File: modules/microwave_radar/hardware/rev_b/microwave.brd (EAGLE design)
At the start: 68.1 x 66 mm, 56 parts, among them J1 MODULE_GENERIC, J2 TC2030-JLINK-L, U1 SAM4LC8AA, U2 TLV62130, U3 MSGEQ7, U4 HB100, U5 OP284E_SEPARATE

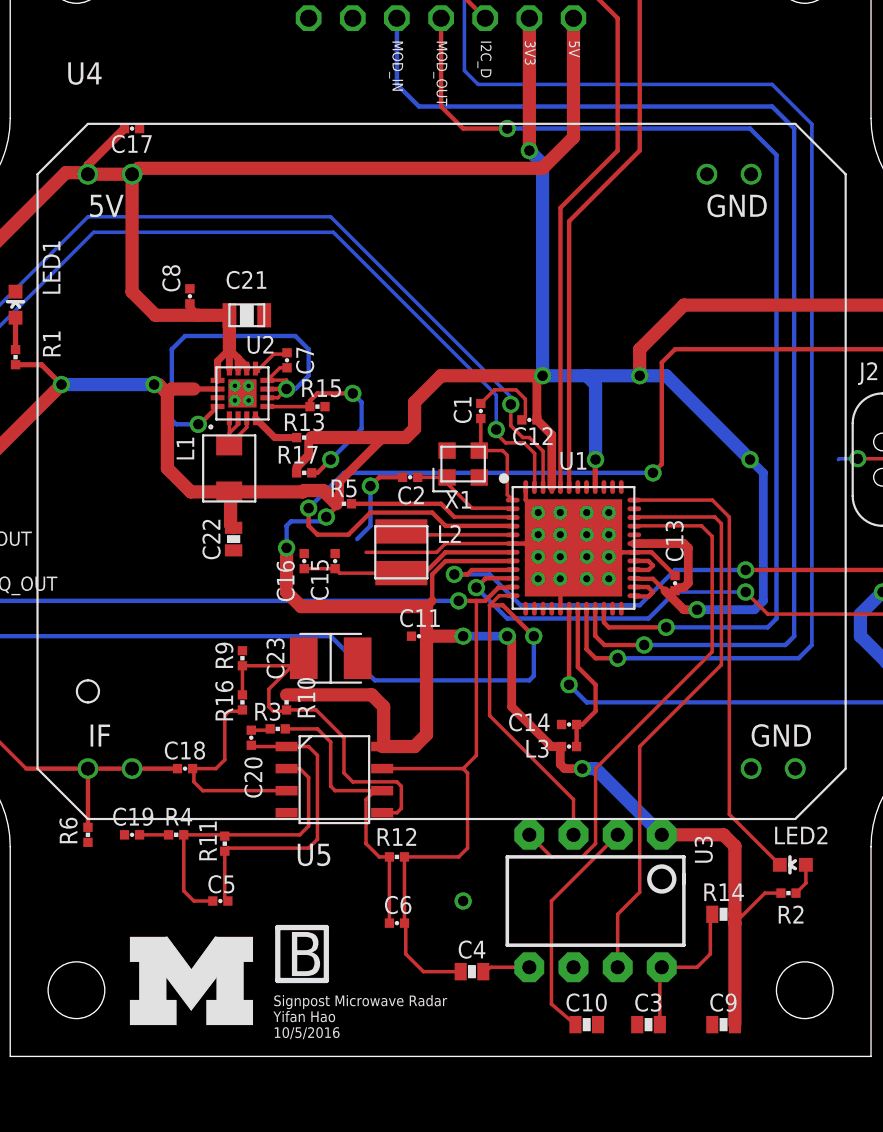
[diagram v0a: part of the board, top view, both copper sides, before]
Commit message: Fix MSGEQ7 swapped pins!!!
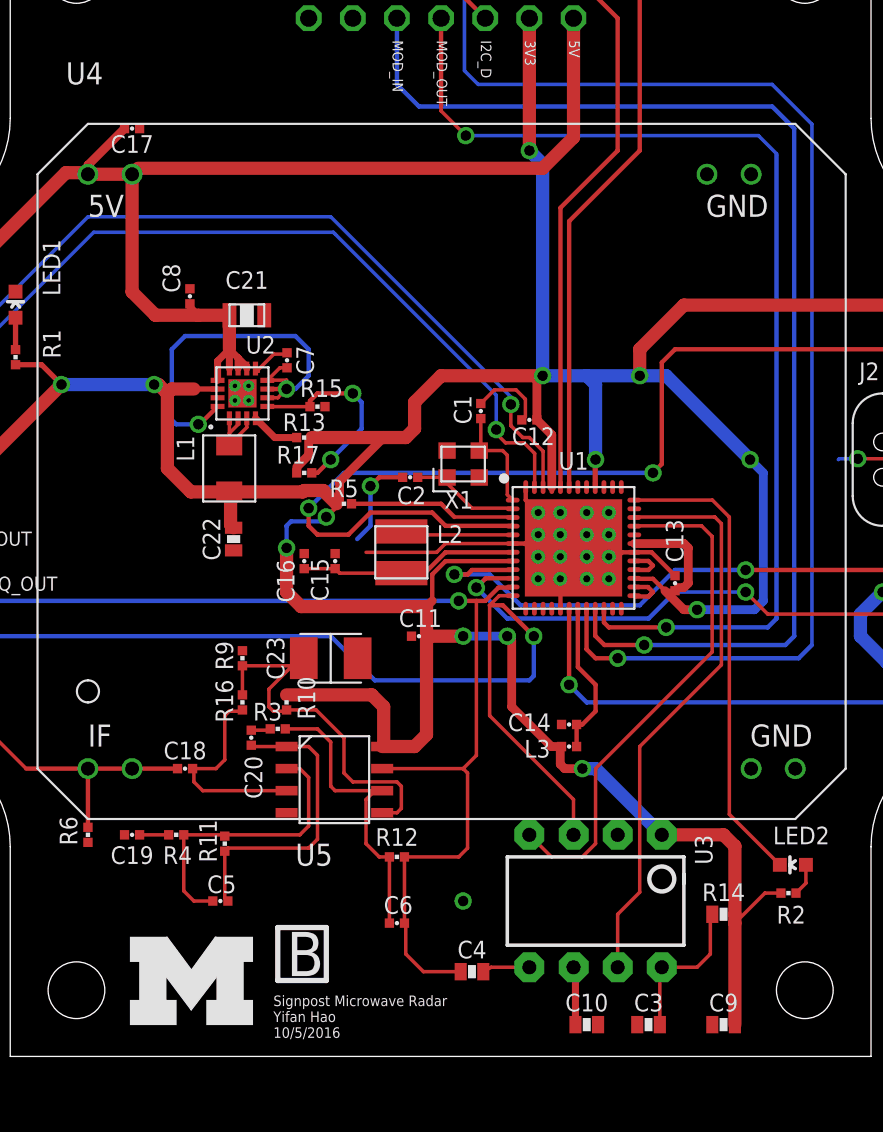
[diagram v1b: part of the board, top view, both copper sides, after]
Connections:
- net GND: now also U3.2; no longer U3.6
- net N$7: now also U3.6; no longer U3.2
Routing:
- net N$7: track 13.1 -> 3.41 mm
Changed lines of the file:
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@@
 </element>
 <element name="R4" library="passives" package="0402_RES" value="10k" x="21.59" y="15.24" smashed="yes" rot="R180">
-<attribute name="NAME" x="21.7424" y="16.7894" size="1.016" layer="25" font="vector" ratio="12" rot="R180" align="bottom-center"/>
+<attribute name="NAME" x="21.6662" y="14.5796" size="1.016" layer="25" font="vector" ratio="12" rot="R180" align="bottom-center"/>
 <attribute name="VALUE" x="21.59" y="16.637" size="1.016" layer="27" font="vector" ratio="12" rot="R180" align="bottom-center"/>
 <attribute name="DIGIKEY" value="1276-3431-1-ND" x="21.59" y="15.24" size="1.778" layer="27" rot="R180" display="off"/>
 </element>
 <element name="C19" library="passives" package="0402_CAP" value="4.7uF" x="19.05" y="15.24" smashed="yes">
-<attribute name="NAME" x="19.1262" y="15.7734" size="1.016" layer="25" font="vector" ratio="12" align="bottom-center"/>
+<attribute name="NAME" x="19.05" y="13.5636" size="1.016" layer="25" font="vector" ratio="12" align="bottom-center"/>
 <attribute name="DIGIKEY" value="1276-1481-1-ND" x="19.05" y="15.24" size="1.778" layer="27" display="off"/>
 </element>
@@
 <contactref element="U2" pad="6"/>
 <contactref element="R15" pad="1"/>
-<contactref element="U3" pad="6"/>
 <wire x1="47.954" y1="31.496" x2="47.95" y2="31.5" width="0.2032" layer="1"/>
 <polygon width="0.2032" layer="1" isolate="0.254">
@@
 <contactref element="C9" pad="1"/>
 <contactref element="C3" pad="2"/>
-<contactref element="C10" pad="2"/>
 <via x="38.1" y="11.43" extent="1-16" drill="0.6"/>
 <wire x1="27.9654" y1="42.11193125" x2="27.55193125" y2="42.11193125" width="0.2032" layer="1"/>
@@
 <wire x1="41.6814" y1="39.32046875" x2="41.47693125" y2="39.116" width="0.2032" layer="1"/>
 <contactref element="LED1" pad="C"/>
+<contactref element="C10" pad="2"/>
+<contactref element="U3" pad="2"/>
 </signal>
 <signal name="CONTROLLER_XIN">
@@
 <wire x1="55.626" y1="27.178" x2="56.134" y2="27.686" width="0.254" layer="16"/>
 <wire x1="56.134" y1="27.686" x2="56.134" y2="54.356" width="0.254" layer="16"/>
-<wire x1="56.134" y1="54.356" x2="54.61" y2="55.88" width="0.254" layer="16"/>
-<wire x1="54.61" y1="55.88" x2="40.64" y2="55.88" width="0.254" layer="16"/>
-<via x="40.64" y="55.88" extent="1-16" drill="0.6"/>
-<wire x1="40.64" y1="55.88" x2="38.1" y2="55.88" width="0.254" layer="1"/>
-<wire x1="38.1" y1="55.88" x2="36.83" y2="57.15" width="0.254" layer="1"/>
 <wire x1="36.83" y1="57.15" x2="36.83" y2="62.23" width="0.254" layer="1"/>
+<wire x1="56.134" y1="54.356" x2="56.134" y2="54.4322" width="0.2032" layer="16"/>
+<wire x1="56.134" y1="54.4322" x2="55.0926" y2="55.4736" width="0.2032" layer="16"/>
+<wire x1="55.0926" y1="55.4736" x2="38.2524" y2="55.4736" width="0.2032" layer="16"/>
+<via x="38.2524" y="55.4736" extent="1-16" drill="0.6"/>
+<wire x1="38.2524" y1="55.4736" x2="36.83" y2="56.896" width="0.2032" layer="1"/>
+<wire x1="36.83" y1="56.896" x2="36.83" y2="57.15" width="0.2032" layer="1"/>
 </signal>
 <signal name="AMP_OUT">
@@
 <wire x1="49.418" y1="7.332" x2="49.418" y2="4.318" width="0.2032" layer="1"/>
 </signal>
-<signal name="N$7">
-<contactref element="U3" pad="2"/>
-<wire x1="43.18" y1="11.43" x2="46.99" y2="15.24" width="0.2032" layer="1"/>
-<contactref element="C10" pad="1"/>
-<wire x1="43.18" y1="11.43" x2="43.18" y2="5.5" width="0.2032" layer="1"/>
-<wire x1="43.18" y1="5.5" x2="44.562" y2="4.318" width="0.2032" layer="1"/>
-</signal>
 <signal name="N$4">
 <contactref element="R1" pad="2"/>
@@
 <wire x1="53.4162" y1="16.4204" x2="56.3238" y2="13.5128" width="0.2032" layer="1"/>
 </signal>
+<signal name="N$7">
+<contactref element="U3" pad="6"/>
+<contactref element="C10" pad="1"/>
+<wire x1="44.45" y1="7.62" x2="44.562" y2="7.62" width="0.4064" layer="1"/>
+<wire x1="44.562" y1="7.62" x2="44.562" y2="4.318" width="0.4064" layer="1"/>
+</signal>
 </signals>

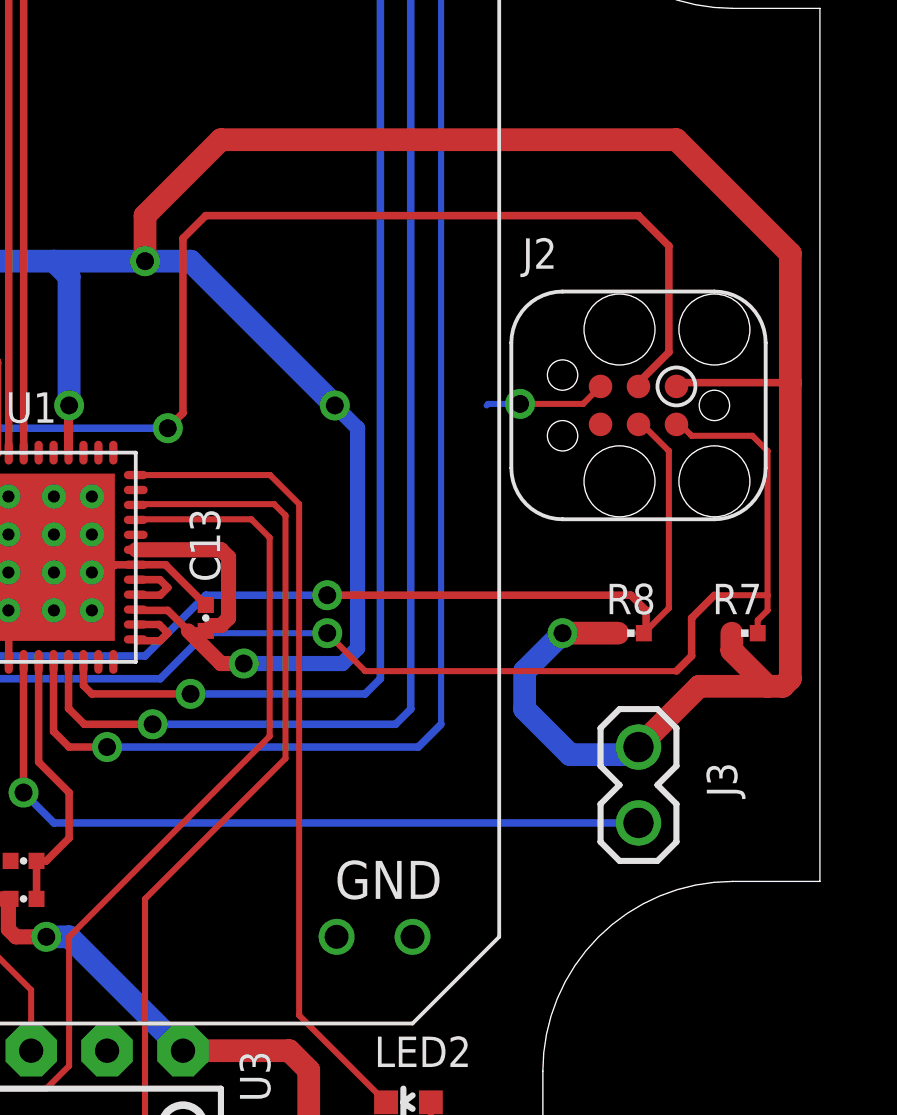
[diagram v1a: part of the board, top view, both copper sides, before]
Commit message: Add vias for gnd layer
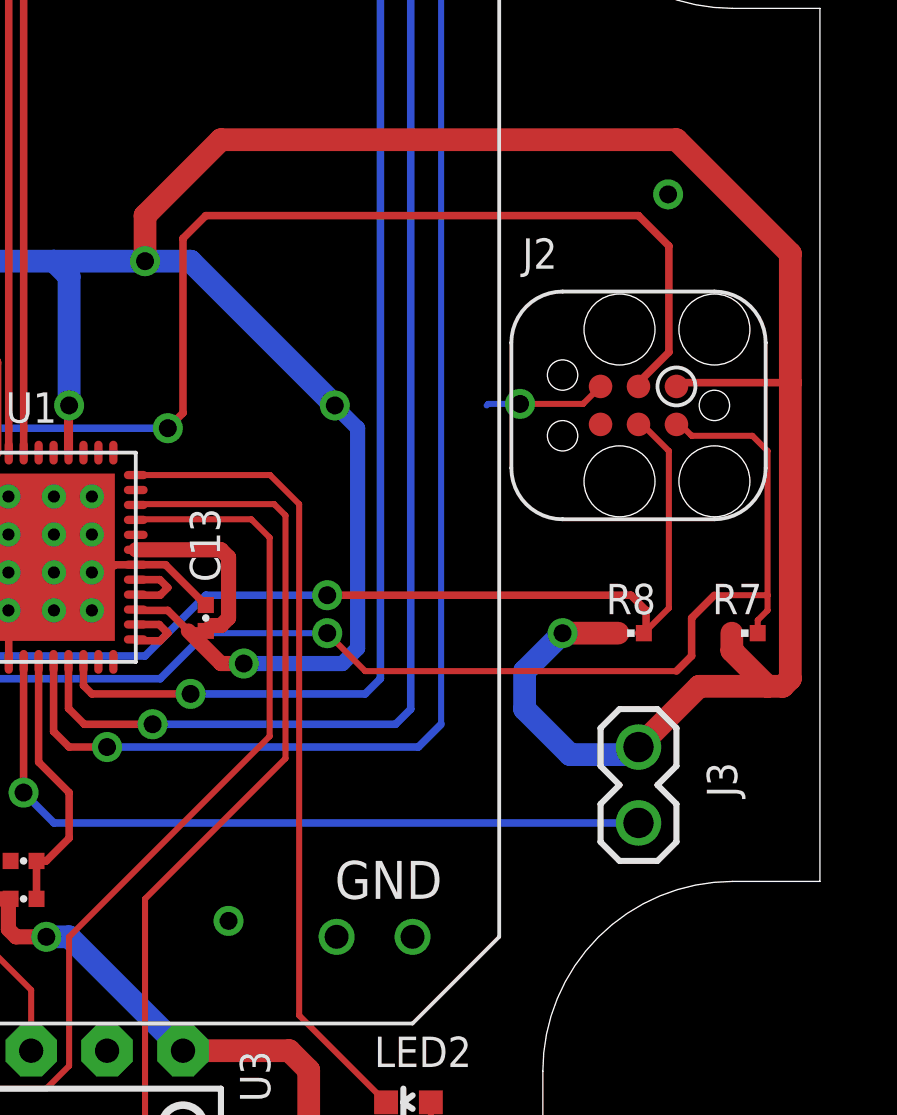
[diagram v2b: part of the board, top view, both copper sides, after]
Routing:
- net GND: vias 25 -> 27
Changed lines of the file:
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@@
 <contactref element="C10" pad="2"/>
 <contactref element="U3" pad="2"/>
+<via x="65.7606" y="43.8912" extent="1-16" drill="0.6"/>
+<via x="51.054" y="19.5834" extent="1-16" drill="0.6"/>
 </signal>
 <signal name="CONTROLLER_XIN">

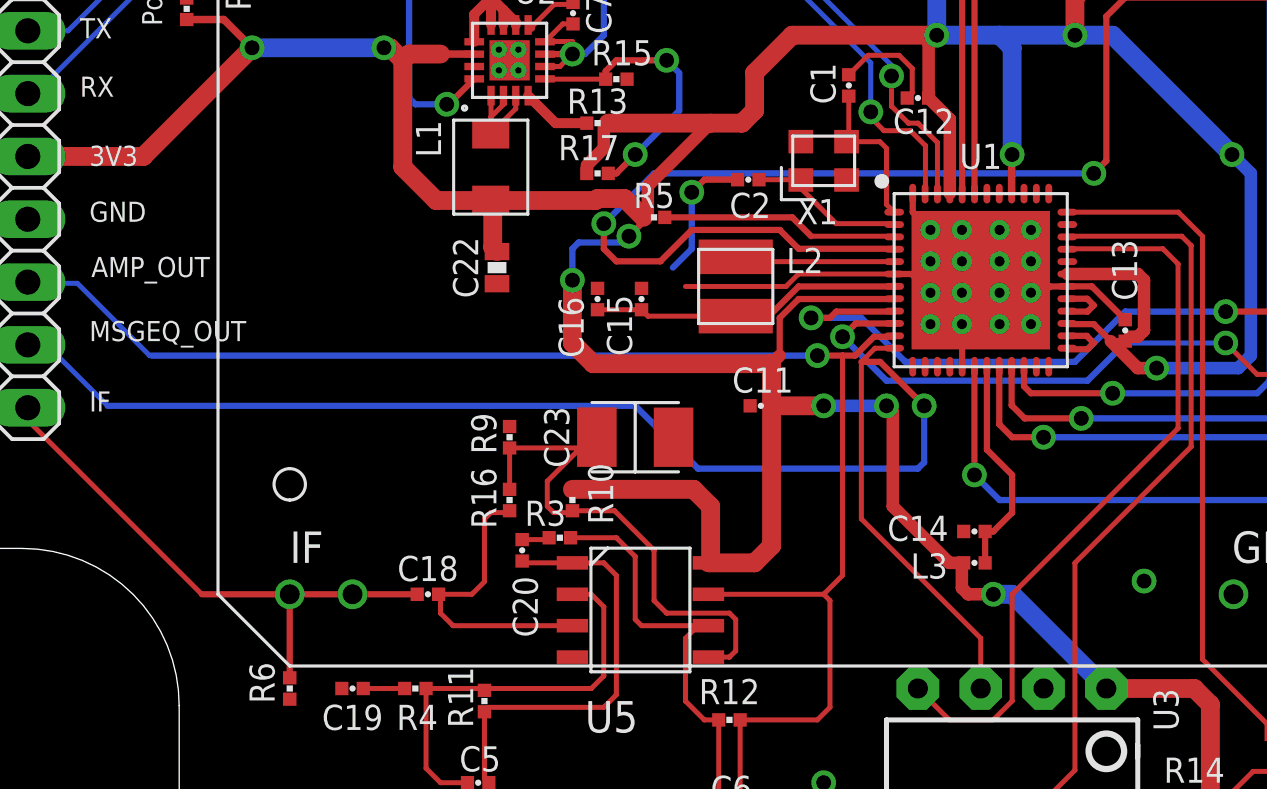
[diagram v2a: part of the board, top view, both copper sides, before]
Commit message: moved switching regulator caps
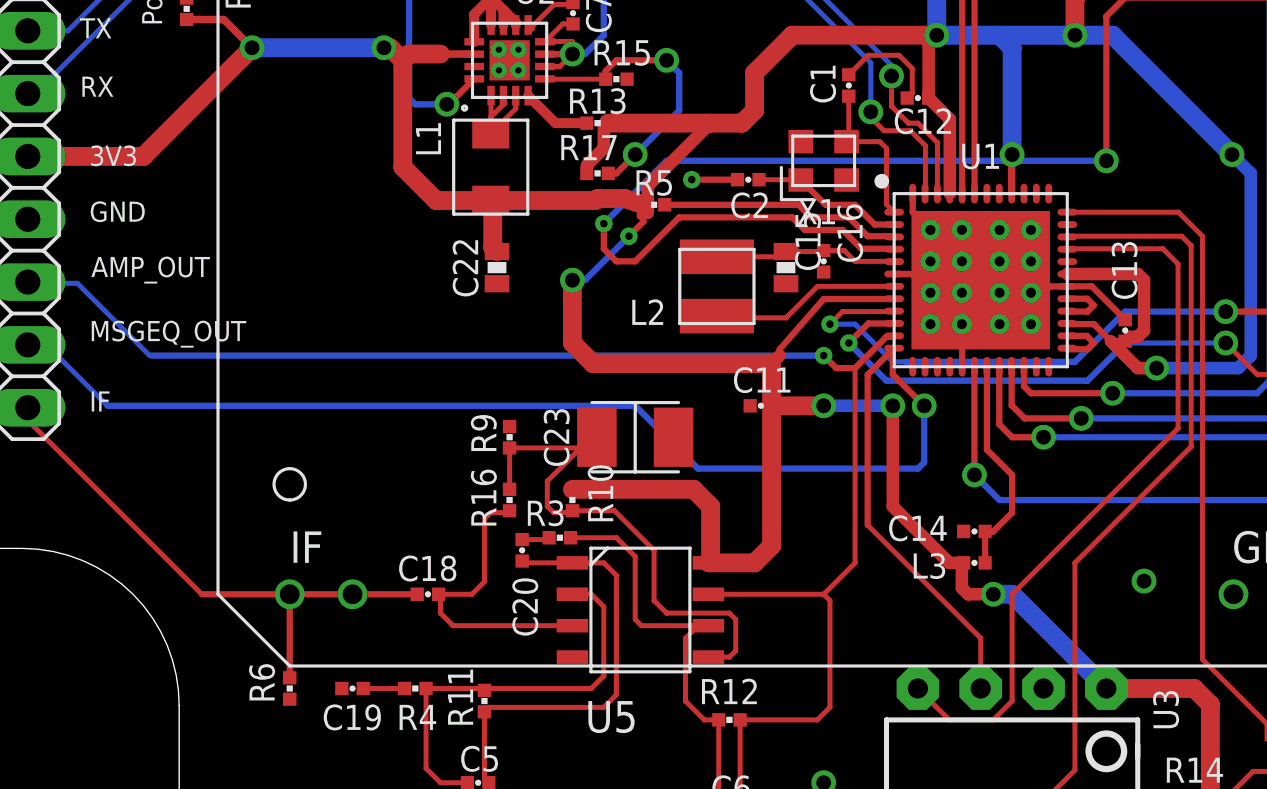
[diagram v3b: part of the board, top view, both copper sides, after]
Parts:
- C15: value 4.7uF -> 6.8uF; device passives:0402_CAP -> passives:0603_CAP
- moved C16 9.27 mm to (38.1, 32.5), turned to 90 degrees
- moved C15 5.98 mm to (36.6, 32.3), turned to 90 degrees
- moved L2 0.76 mm to (33.8, 31.5), turned to 270 degrees
- moved R5 0.51 mm to (31.2, 34.8)
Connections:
- removed net N$5: L2.P$2, U1.5
- new net N$36: C15.2, C16.2, L2.P$1, U1.5
- net N$6: now also L2.P$2; no longer C15.2, C16.2, L2.P$1
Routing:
- net GND: track 59.0 -> 46.8 mm
- net N$36: track 0.00 -> 7.46 mm
- net N$5: track 6.49 -> 0.00 mm
- net N$6: track 12.7 -> 7.72 mm
- net CONTROLLER_SWDCLK: track 41.9 -> 40.3 mm
- net MSGEQ_OUT: track 60.7 -> 59.6 mm
- net +3V3: track 278.6 -> 278.0 mm
- net CONTROLLER_SWDIO: track 46.1 -> 45.5 mm
